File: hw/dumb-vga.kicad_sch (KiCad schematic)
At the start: 22 parts, among them IC1 74HC590N, IC2 74HC590N, IC3 74HC590N, IC4 74HC574N, P1 CONN_01X03, P2 CONN_01X03, P3 CONN_01X03, U1 A29040C, X1 VGAF

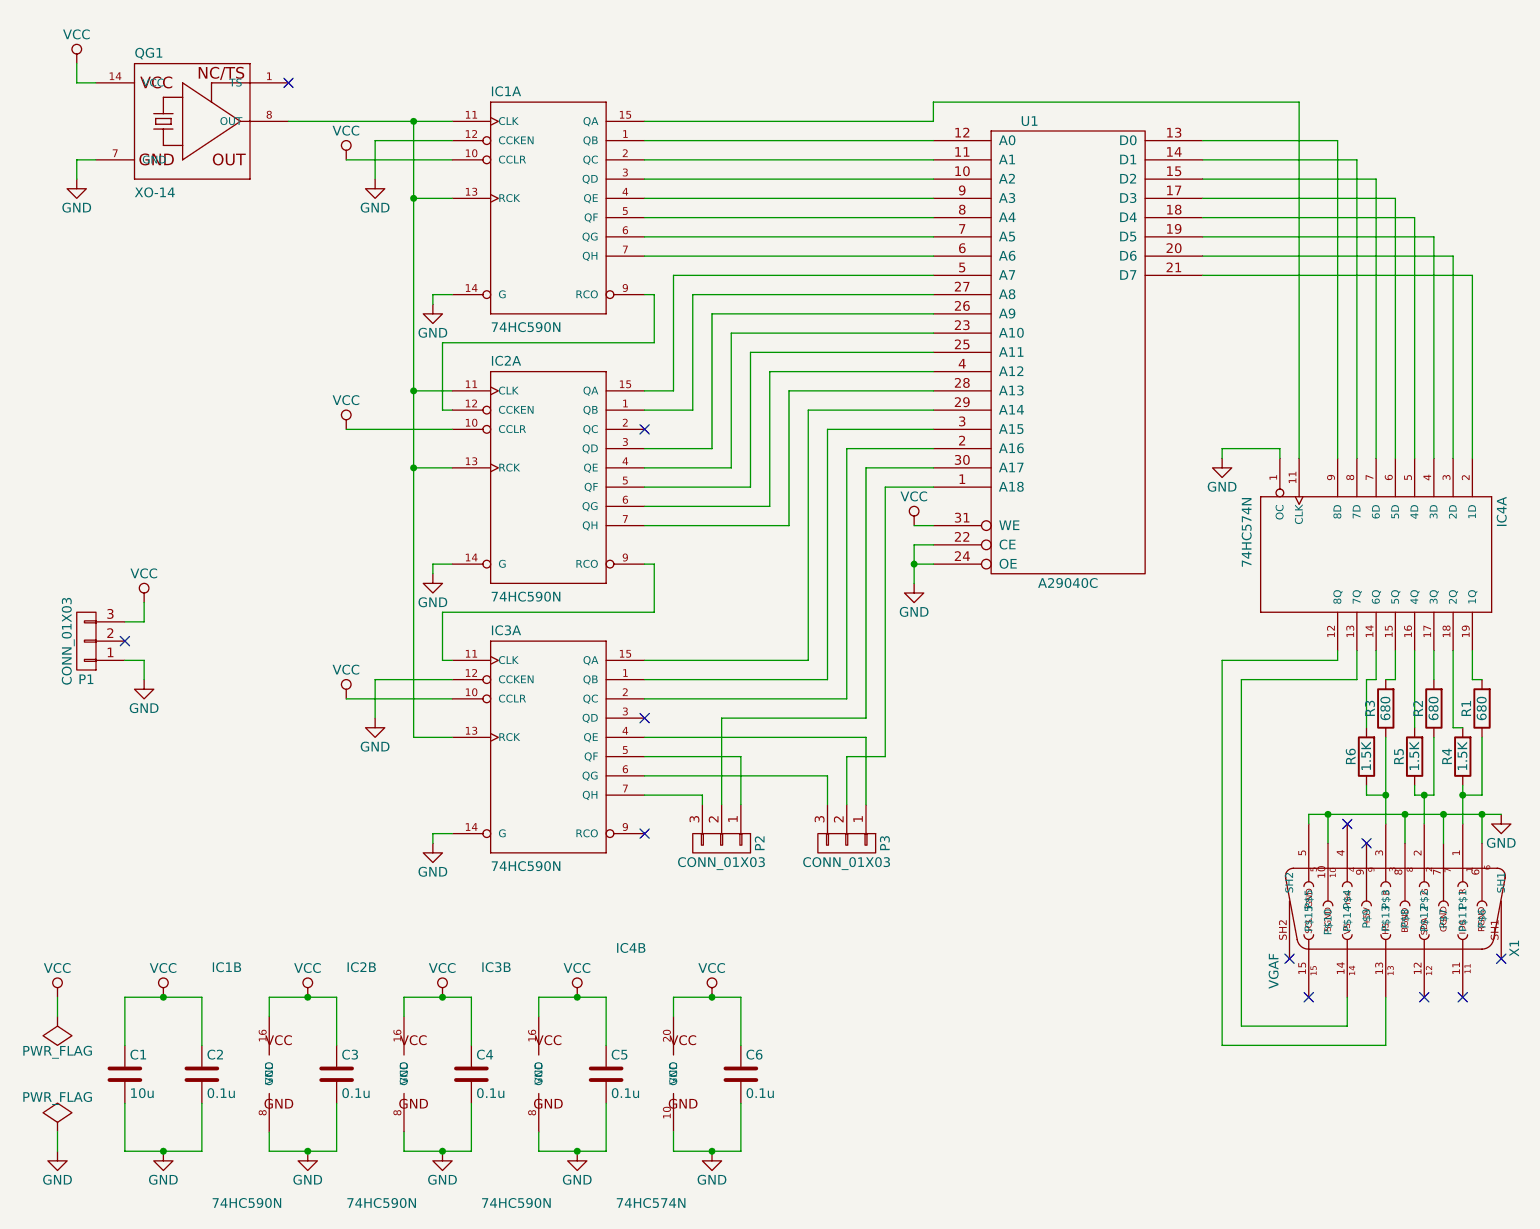
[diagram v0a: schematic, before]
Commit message: Move away from custom symbols, where convenient.
Upgrading from an ancient version of Kicad left me with a bunch of
symbosls in a local library that overlapped with the standard
library. For the easy cases, I've tried to switch over. Where it would
require rearranging lines on the schematic, I have not bothered.
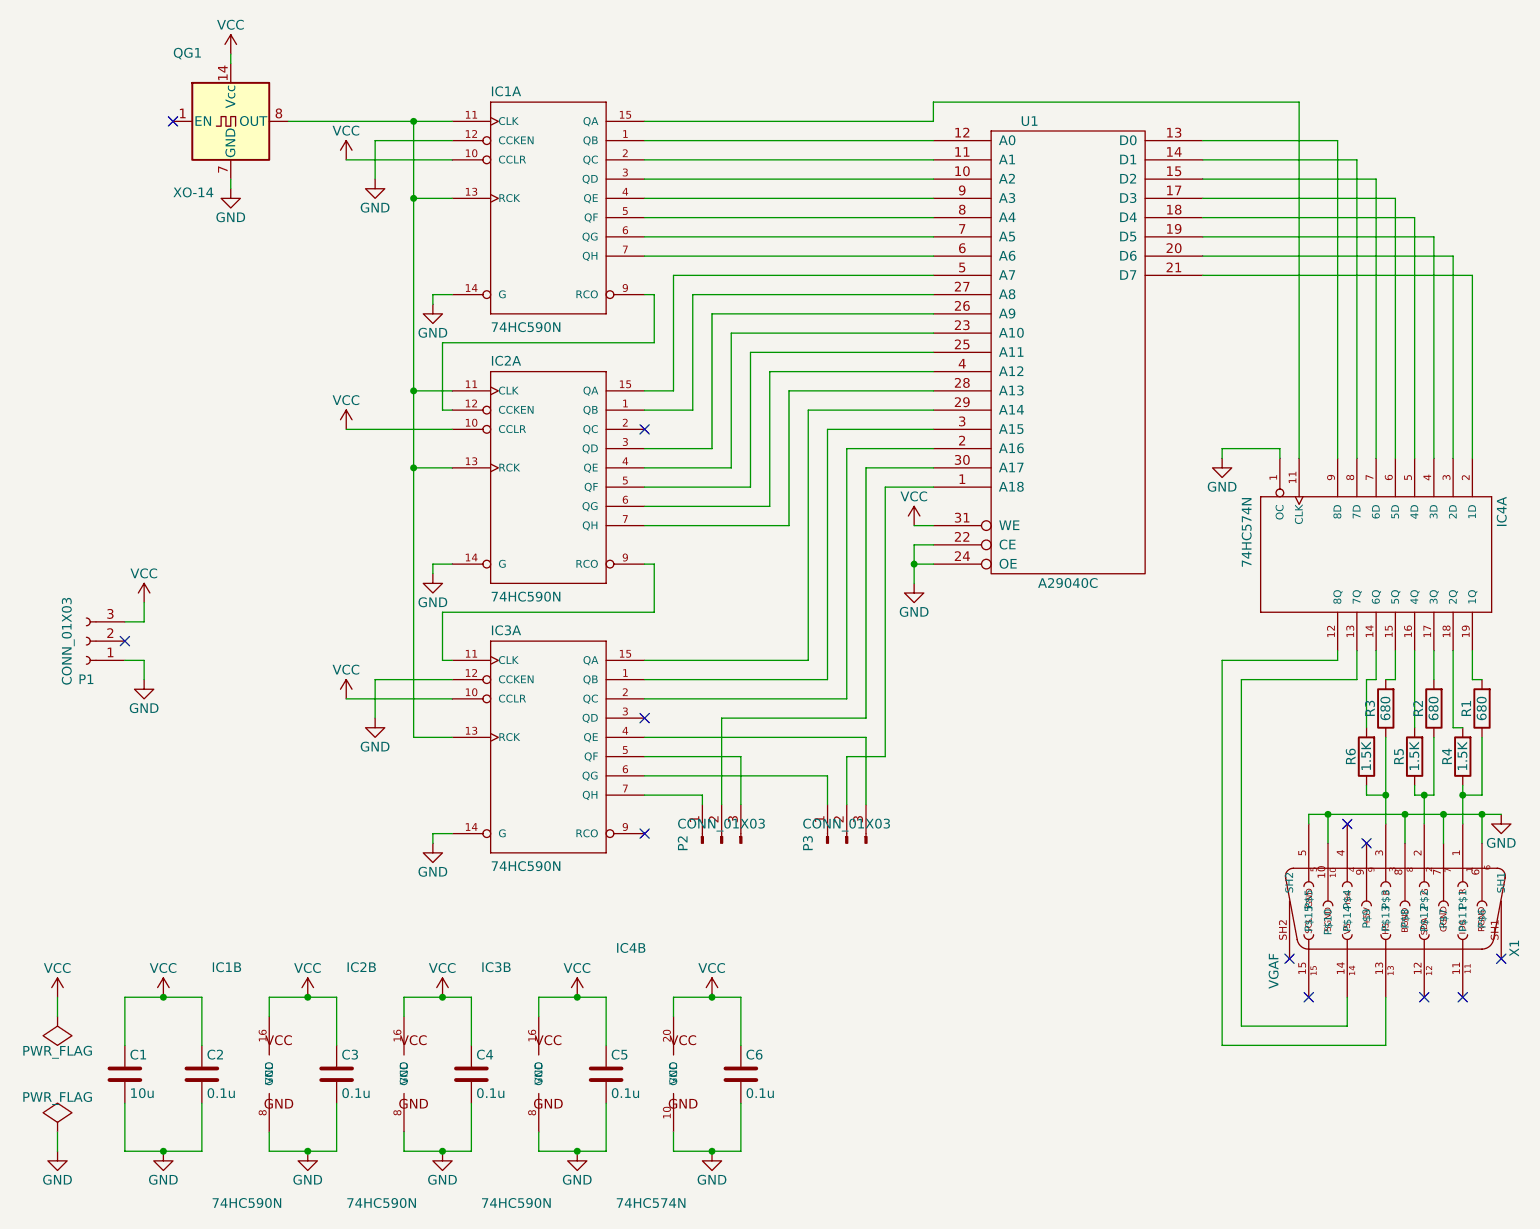
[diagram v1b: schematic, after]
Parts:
- C1, C2, C3, C4, C5, C6: symbol dumb-vga-rescue:C -> Device:C
- P1: symbol dumb-vga-rescue:CONN_01X03 -> Connector:Conn_01x03_Socket
- P2, P3: symbol dumb-vga-rescue:CONN_01X03 -> Connector:Conn_01x03_Pin
- QG1: symbol dumb-vga-rescue:XO-14 -> Oscillator:CXO_DIP14
- R1, R2, R3, R4, R5, R6: symbol dumb-vga-rescue:R -> Device:R
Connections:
- net at IC3.4 (QE): now also P3.3 (Pin_3); no longer P3.1 (P1)
- net at IC3.5 (QF): now also P2.3 (Pin_3); no longer P2.1 (P1)
- net at IC3.6 (QG): now also P3.1 (Pin_1); no longer P3.3 (P3)
- net at IC3.7 (QH): now also P2.1 (Pin_1); no longer P2.3 (P3)

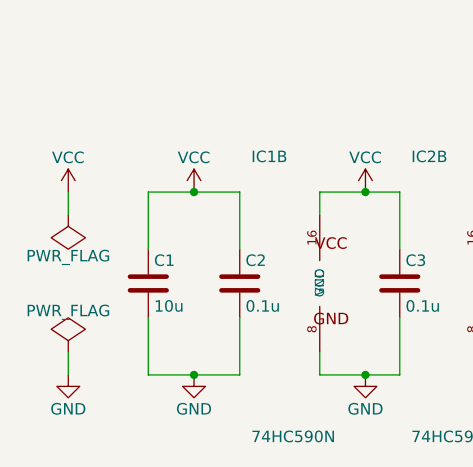
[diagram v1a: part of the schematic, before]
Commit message: Move PCB onto standard footprints
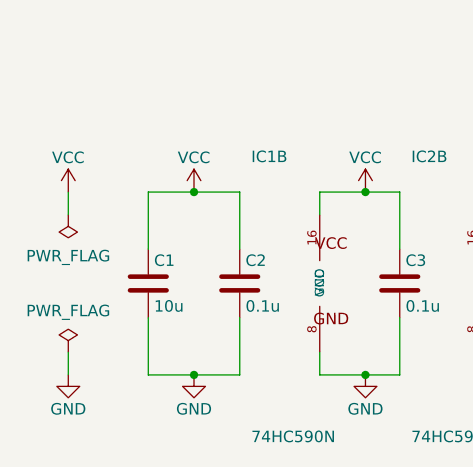
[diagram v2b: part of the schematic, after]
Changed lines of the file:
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@@
     )
   )
-  (symbol (lib_id "dumb-vga-rescue:PWR_FLAG") (at 21.59 153.67 180) (unit 1)
+  (symbol (lib_id "power:PWR_FLAG") (at 21.59 153.67 180) (unit 1)
     (in_bom yes) (on_board yes) (dnp no)
     (property "Reference" "#FLG020" (at 21.59 156.083 0)
@@
     )
     (property "Footprint" "" (at 21.59 153.67 0)
-      (effects (font (size 1.27 1.27)))
+      (effects (font (size 1.27 1.27)) hide)
     )
-    (property "Datasheet" "" (at 21.59 153.67 0)
-      (effects (font (size 1.27 1.27)))
+    (property "Datasheet" "~" (at 21.59 153.67 0)
+      (effects (font (size 1.27 1.27)) hide)
     )
     (pin "1")
@@
     )
   )
-  (symbol (lib_id "dumb-vga-rescue:PWR_FLAG") (at 21.59 168.91 0) (unit 1)
+  (symbol (lib_id "power:PWR_FLAG") (at 21.59 168.91 0) (unit 1)
     (in_bom yes) (on_board yes) (dnp no)
     (property "Reference" "#FLG023" (at 21.59 166.497 0)
@@
     )
     (property "Footprint" "" (at 21.59 168.91 0)
-      (effects (font (size 1.27 1.27)))
+      (effects (font (size 1.27 1.27)) hide)
     )
-    (property "Datasheet" "" (at 21.59 168.91 0)
-      (effects (font (size 1.27 1.27)))
+    (property "Datasheet" "~" (at 21.59 168.91 0)
+      (effects (font (size 1.27 1.27)) hide)
     )
     (pin "1")

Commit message: Update project-specific library
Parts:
- IC1, IC2, IC3: footprint Housings_DIP:DIP-16_W7.62mm -> 74xx-eu-DIL16
- IC4: footprint Housings_DIP:DIP-20_W7.62mm -> 74xx-eu-DIL20
- QG1: footprint hw:xo-8-14 -> Oscillator:Oscillator_DIP-14
- X1: footprint hw:hd15f -> HD15_B-HD15F
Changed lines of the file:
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@@
       (effects (font (size 1.27 1.27)) (justify left bottom))
     )
-    (property "Footprint" "Housings_DIP:DIP-16_W7.62mm" (at 86.36 41.91 0)
+    (property "Footprint" "74xx-eu-DIL16" (at 86.36 41.91 0)
       (effects (font (size 1.27 1.27)) hide)
     )
@@
       (effects (font (size 1.27 1.27)) (justify left bottom))
     )
-    (property "Footprint" "Housings_DIP:DIP-16_W7.62mm" (at 49.53 157.48 0)
+    (property "Footprint" "74xx-eu-DIL16" (at 49.53 157.48 0)
       (effects (font (size 1.27 1.27)) hide)
     )
@@
       (effects (font (size 1.27 1.27)) (justify left bottom))
     )
-    (property "Footprint" "Housings_DIP:DIP-16_W7.62mm" (at 67.31 157.48 0)
+    (property "Footprint" "74xx-eu-DIL16" (at 67.31 157.48 0)
       (effects (font (size 1.27 1.27)) hide)
     )
@@
       (effects (font (size 1.27 1.27)) (justify left bottom))
     )
-    (property "Footprint" "Housings_DIP:DIP-16_W7.62mm" (at 85.09 157.48 0)
+    (property "Footprint" "74xx-eu-DIL16" (at 85.09 157.48 0)
       (effects (font (size 1.27 1.27)) hide)
     )
@@
       (effects (font (size 1.27 1.27)) (justify left bottom))
     )
-    (property "Footprint" "Housings_DIP:DIP-16_W7.62mm" (at 86.36 77.47 0)
+    (property "Footprint" "74xx-eu-DIL16" (at 86.36 77.47 0)
       (effects (font (size 1.27 1.27)) hide)
     )
@@
       (effects (font (size 1.27 1.27)) (justify left bottom))
     )
-    (property "Footprint" "Housings_DIP:DIP-16_W7.62mm" (at 86.36 113.03 0)
+    (property "Footprint" "74xx-eu-DIL16" (at 86.36 113.03 0)
       (effects (font (size 1.27 1.27)) hide)
     )
@@
       (effects (font (size 1.27 1.27)) (justify left bottom))
     )
-    (property "Footprint" "hw:hd15f" (at 203.2 138.43 0)
+    (property "Footprint" "HD15_B-HD15F" (at 203.2 138.43 0)
       (effects (font (size 1.27 1.27)) hide)
     )
@@
       (effects (font (size 1.27 1.27)) (justify left bottom))
     )
-    (property "Footprint" "Housings_DIP:DIP-20_W7.62mm" (at 199.39 92.71 0)
+    (property "Footprint" "74xx-eu-DIL20" (at 199.39 92.71 0)
       (effects (font (size 1.27 1.27)) hide)
     )
@@
       (effects (font (size 1.27 1.27)) (justify left bottom))
     )
-    (property "Footprint" "Housings_DIP:DIP-20_W7.62mm" (at 102.87 157.48 0)
+    (property "Footprint" "74xx-eu-DIL20" (at 102.87 157.48 0)
       (effects (font (size 1.27 1.27)) hide)
     )
@@
       (effects (font (size 1.27 1.27)) (justify left bottom))
     )
-    (property "Footprint" "hw:xo-8-14" (at 55.88 44.45 0)
-      (effects (font (size 1.27 1.27)) hide)
-    )
+    (property "Footprint" "Oscillator:Oscillator_DIP-14" (at 55.88 44.45 0)
+      (effects (font (size 1.27 1.27)) hide)
+    )

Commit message: Rename the library, to no longer be "rescue".
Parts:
- IC1, IC2, IC3: footprint 74xx-eu-DIL16 -> Package_DIP:DIP-16_W7.62mm; symbol dumb-vga-rescue:74HC590N -> dumb-vga:74HC590N
- IC4: footprint 74xx-eu-DIL20 -> Package_DIP:DIP-20_W7.62mm; symbol dumb-vga-rescue:74HC574N -> dumb-vga:74HC574N
- U1: footprint Housings_DIP:DIP-32_W15.24mm -> Package_DIP:DIP-32_W15.24mm; symbol dumb-vga-rescue:A29040C -> dumb-vga:A29040C
- X1: footprint HD15_B-HD15F -> hw:hd15f; symbol dumb-vga-rescue:VGAF -> dumb-vga:VGAF
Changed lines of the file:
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@@
     (stroke (width 0) (type default))
   )
-  (symbol (lib_id "dumb-vga-rescue:74HC590N") (at 86.36 45.72 0) (unit 1)
+  (symbol (lib_id "dumb-vga:74HC590N") (at 86.36 45.72 0) (unit 1)
     (in_bom yes) (on_board yes) (dnp no)
     (property "Reference" "IC1" (at 78.74 32.385 0)
@@
       (effects (font (size 1.27 1.27)) (justify left bottom))
     )
-    (property "Footprint" "74xx-eu-DIL16" (at 86.36 41.91 0)
+    (property "Footprint" "Package_DIP:DIP-16_W7.62mm" (at 86.36 41.91 0)
       (effects (font (size 1.27 1.27)) hide)
     )
@@
     )
   )
-  (symbol (lib_id "dumb-vga-rescue:74HC590N") (at 49.53 161.29 0) (unit 2)
+  (symbol (lib_id "dumb-vga:74HC590N") (at 49.53 161.29 0) (unit 2)
     (in_bom yes) (on_board yes) (dnp no)
     (property "Reference" "IC1" (at 41.91 147.955 0)
@@
       (effects (font (size 1.27 1.27)) (justify left bottom))
     )
-    (property "Footprint" "74xx-eu-DIL16" (at 49.53 157.48 0)
+    (property "Footprint" "Package_DIP:DIP-16_W7.62mm" (at 49.53 157.48 0)
       (effects (font (size 1.27 1.27)) hide)
     )
@@
     )
   )
-  (symbol (lib_id "dumb-vga-rescue:74HC590N") (at 67.31 161.29 0) (unit 2)
+  (symbol (lib_id "dumb-vga:74HC590N") (at 67.31 161.29 0) (unit 2)
     (in_bom yes) (on_board yes) (dnp no)
     (property "Reference" "IC2" (at 59.69 147.955 0)
@@
       (effects (font (size 1.27 1.27)) (justify left bottom))
     )
-    (property "Footprint" "74xx-eu-DIL16" (at 67.31 157.48 0)
+    (property "Footprint" "Package_DIP:DIP-16_W7.62mm" (at 67.31 157.48 0)
       (effects (font (size 1.27 1.27)) hide)
     )
@@
     )
   )
-  (symbol (lib_id "dumb-vga-rescue:74HC590N") (at 85.09 161.29 0) (unit 2)
+  (symbol (lib_id "dumb-vga:74HC590N") (at 85.09 161.29 0) (unit 2)
     (in_bom yes) (on_board yes) (dnp no)
     (property "Reference" "IC3" (at 77.47 147.955 0)
@@
       (effects (font (size 1.27 1.27)) (justify left bottom))
     )
-    (property "Footprint" "74xx-eu-DIL16" (at 85.09 157.48 0)
+    (property "Footprint" "Package_DIP:DIP-16_W7.62mm" (at 85.09 157.48 0)
       (effects (font (size 1.27 1.27)) hide)
     )
@@
     )
   )
-  (symbol (lib_id "dumb-vga-rescue:74HC590N") (at 86.36 81.28 0) (unit 1)
+  (symbol (lib_id "dumb-vga:74HC590N") (at 86.36 81.28 0) (unit 1)
     (in_bom yes) (on_board yes) (dnp no)
     (property "Reference" "IC2" (at 78.74 67.945 0)
@@
       (effects (font (size 1.27 1.27)) (justify left bottom))
     )
-    (property "Footprint" "74xx-eu-DIL16" (at 86.36 77.47 0)
+    (property "Footprint" "Package_DIP:DIP-16_W7.62mm" (at 86.36 77.47 0)
       (effects (font (size 1.27 1.27)) hide)
     )
@@
     )
   )
-  (symbol (lib_id "dumb-vga-rescue:74HC590N") (at 86.36 116.84 0) (unit 1)
+  (symbol (lib_id "dumb-vga:74HC590N") (at 86.36 116.84 0) (unit 1)
     (in_bom yes) (on_board yes) (dnp no)
     (property "Reference" "IC3" (at 78.74 103.505 0)
@@
       (effects (font (size 1.27 1.27)) (justify left bottom))
     )
-    (property "Footprint" "74xx-eu-DIL16" (at 86.36 113.03 0)
+    (property "Footprint" "Package_DIP:DIP-16_W7.62mm" (at 86.36 113.03 0)
       (effects (font (size 1.27 1.27)) hide)
     )
@@
     )
   )
-  (symbol (lib_id "dumb-vga-rescue:VGAF") (at 199.39 138.43 270) (unit 1)
+  (symbol (lib_id "dumb-vga:VGAF") (at 199.39 138.43 270) (unit 1)
     (in_bom yes) (on_board yes) (dnp no)
     (property "Reference" "X1" (at 213.106 143.51 0)
@@
       (effects (font (size 1.27 1.27)) (justify left bottom))
     )
-    (property "Footprint" "HD15_B-HD15F" (at 203.2 138.43 0)
+    (property "Footprint" "hw:hd15f" (at 203.2 138.43 0)
       (effects (font (size 1.27 1.27)) hide)
     )
@@
     )
   )
-  (symbol (lib_id "dumb-vga-rescue:A29040C") (at 154.94 60.96 0) (unit 1)
+  (symbol (lib_id "dumb-vga:A29040C") (at 154.94 60.96 0) (unit 1)
     (in_bom yes) (on_board yes) (dnp no)
     (property "Reference" "U1" (at 149.86 35.56 0)
@@
       (effects (font (size 1.27 1.27)))
     )
-    (property "Footprint" "Housings_DIP:DIP-32_W15.24mm" (at 154.94 60.96 0)
+    (property "Footprint" "Package_DIP:DIP-32_W15.24mm" (at 154.94 60.96 0)
       (effects (font (size 1.27 1.27)) hide)
     )
@@
     )
   )
-  (symbol (lib_id "dumb-vga-rescue:74HC574N") (at 195.58 92.71 270) (unit 1)
+  (symbol (lib_id "dumb-vga:74HC574N") (at 195.58 92.71 270) (unit 1)
     (in_bom yes) (on_board yes) (dnp no)
     (property "Reference" "IC4" (at 211.455 85.09 0)
@@
       (effects (font (size 1.27 1.27)) (justify left bottom))
     )
-    (property "Footprint" "74xx-eu-DIL20" (at 199.39 92.71 0)
+    (property "Footprint" "Package_DIP:DIP-20_W7.62mm" (at 199.39 92.71 0)
       (effects (font (size 1.27 1.27)) hide)
     )
@@
     )
   )
-  (symbol (lib_id "dumb-vga-rescue:74HC574N") (at 102.87 161.29 0) (unit 2)
+  (symbol (lib_id "dumb-vga:74HC574N") (at 102.87 161.29 0) (unit 2)
     (in_bom yes) (on_board yes) (dnp no)
     (property "Reference" "IC4" (at 95.25 145.415 0)
@@
       (effects (font (size 1.27 1.27)) (justify left bottom))
     )
-    (property "Footprint" "74xx-eu-DIL20" (at 102.87 157.48 0)
-      (effects (font (size 1.27 1.27)) hide)
-    )
+    (property "Footprint" "Package_DIP:DIP-20_W7.62mm" (at 102.87 157.48 0)
+      (effects (font (size 1.27 1.27)) hide)
+    )
